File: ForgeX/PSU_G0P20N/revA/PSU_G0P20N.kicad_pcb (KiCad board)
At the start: 2 copper layers, 32.1 x 69.8 mm, 49 parts, among them J1 Screw_Terminal_01x02, J2 Conn_02x05_Odd_Even, J4 Conn_01x04, U1 VIPER26LDTR, U2 TL431DBZ, U4 PC817SC_C20612450, U5 MT2492

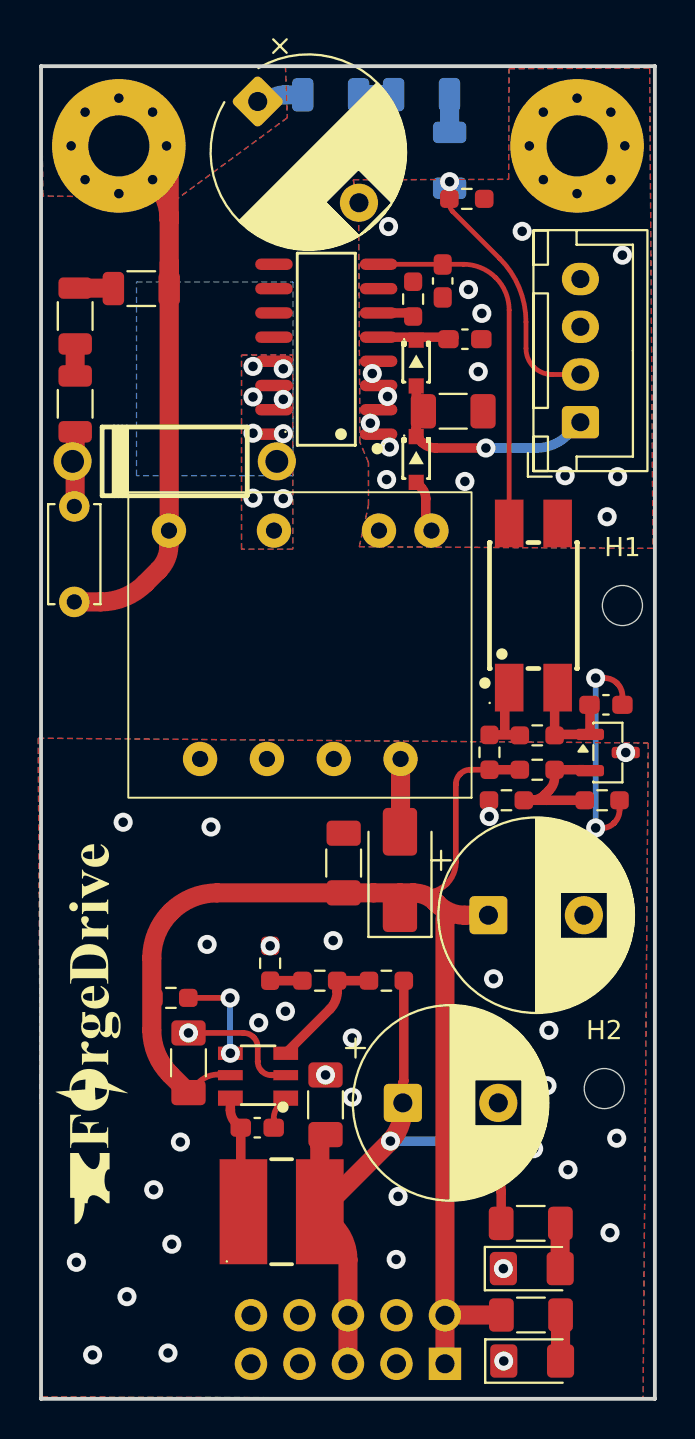
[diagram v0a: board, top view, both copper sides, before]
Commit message: PSU Finalization
PSU Documentation semi finalized, sizing, and schematic and layout second pass semi final updates
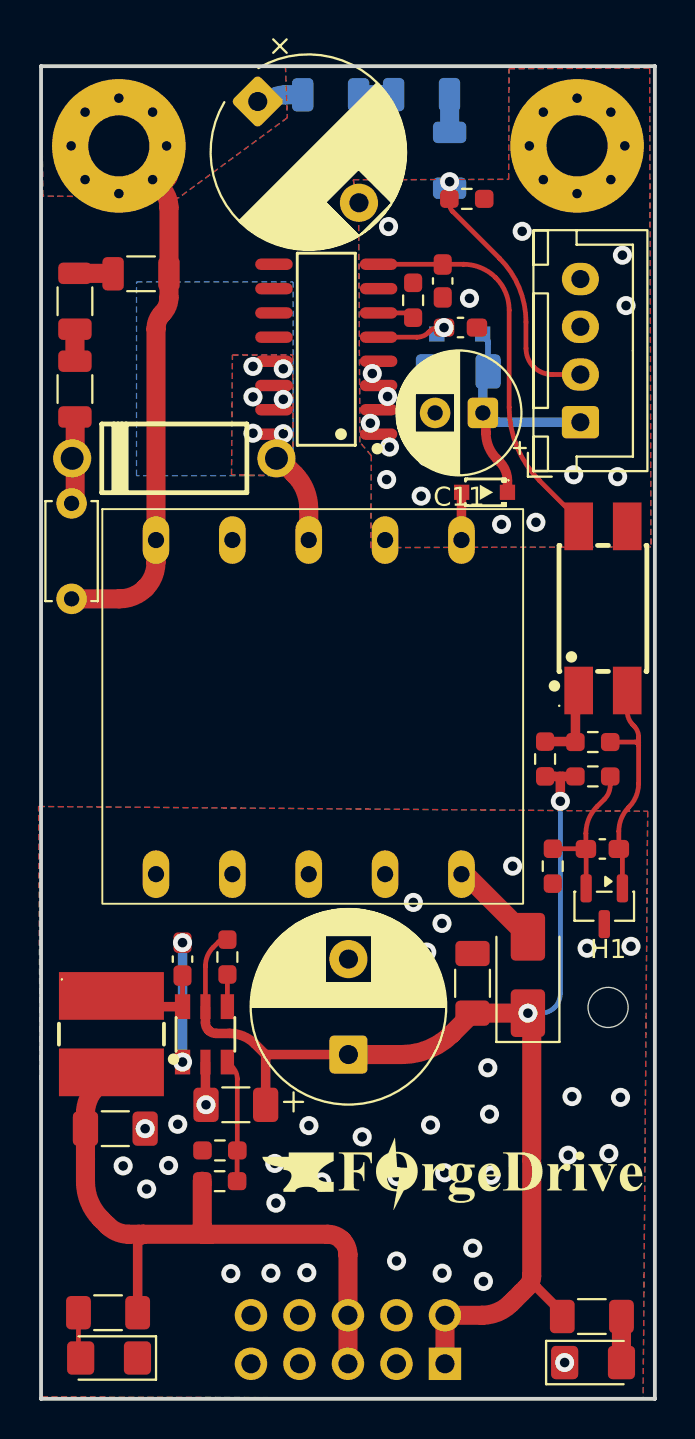
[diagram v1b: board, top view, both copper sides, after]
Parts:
- removed H2: MountingHole, MountingHole:MountingHole_2.1mm
- removed R16: 6.8k, Resistor_SMD:R_0603_1608Metric_Pad0.98x0.95mm_HandSolder
- removed R18: 1k, Resistor_SMD:R_0603_1608Metric_Pad0.98x0.95mm_HandSolder
- C10: value 22u -> 10u
- C11: footprint Capacitor_THT:CP_Radial_D10.0mm_P5.00mm -> Capacitor_THT:CP_Radial_D6.3mm_P2.50mm
- C2: value 100p -> 220nF
- C3, D8: moved to B.Cu
- C4: value 470u -> 2200u
- C5: value 470p -> 2.2n
- L2: value CD54-150M_C49230812 -> CD54-6R8M
- R10, R11, R19: value 10k -> 27k
- R13: value 20k -> 100k
- R14: value 6.8k -> 15k
- R15: value 100k -> 110k
- R7: value 1k -> 1.2k
- R8: value 1k -> 38k
- R9: value 1k -> 10k
- U3: footprint Libmain:E16 Trans -> Libmain:E22 Trans
- moved C11 36.4 mm to (151.5, 69.8), turned to 180 degrees
- moved D4 22.6 mm to (132.0, 119.3), turned to 180 degrees
- moved R1 22.6 mm to (131.9, 116.9), turned to 180 degrees
- moved H1 21.1 mm to (158.1, 100.9)
- moved G*** 20.2 mm to (149.9, 109.6), turned to 0 degrees
- moved R15 13.7 mm to (137.8, 110.0), turned to 0 degrees
- moved L2 12.9 mm to (132.1, 102.3), turned to -90 degrees
- moved C9 11.1 mm to (132.3, 107.3), turned to 0 degrees
- moved C4 10.3 mm to (144.5, 103.4), turned to 90 degrees
- moved R14 10.3 mm to (137.8, 108.4)
- moved C8 9.66 mm to (135.8, 98.4), turned to 90 degrees
- moved C1 9.23 mm to (151.0, 99.6)
- moved D1 8.67 mm to (153.9, 99.2)
- moved U2 8.05 mm to (157.9, 95.6), turned to -90 degrees
- moved C2 7.55 mm to (157.8, 92.6), turned to 0 degrees
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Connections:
- net /FB renamed /COMP
- C11 pad 1: +5V -> /Aux
- C11 pad 2: GND -> GNDPWR
- C2 pad 1: Net-(C2-Pad1) -> Net-(U2-REF)
- R14 pad 2: Net-(R14-Pad2) -> GND
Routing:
- net Net-(C2-Pad1): track 12.7 -> 0.00 mm, vias 2 -> 0
- net Net-(U2-K): track 5.73 -> 12.6 mm
- net GND: track 6.66 -> 1.39 mm, vias 33 -> 39
- net Net-(D3-A): track 0.02 -> 4.86 mm, vias 8 -> 6
- net Net-(U5-BS): track 1.76 -> 6.25 mm, vias 0 -> 2
- net +12V: track 70.0 -> 65.6 mm, vias 0 -> 2
- net /VDCH: track 37.2 -> 33.7 mm
- net Net-(U5-EN): track 5.09 -> 1.69 mm, vias 2 -> 0
- net /Aux: track 12.0 -> 14.0 mm, vias 1 -> 0
- net Net-(D1-A): track 3.01 -> 4.83 mm
- net Net-(R14-Pad2): track 1.69 -> 0.00 mm
- net +5V: track 36.8 -> 35.4 mm, vias 2 -> 0
- net /COMP: track 19.4 -> 20.7 mm
- net Net-(D3-C): track 3.92 -> 4.70 mm
- net Net-(U2-REF): track 7.25 -> 8.01 mm
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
